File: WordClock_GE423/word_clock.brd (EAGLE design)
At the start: 100 x 76.2 mm, 45 parts, among them Q1 32.768kHz

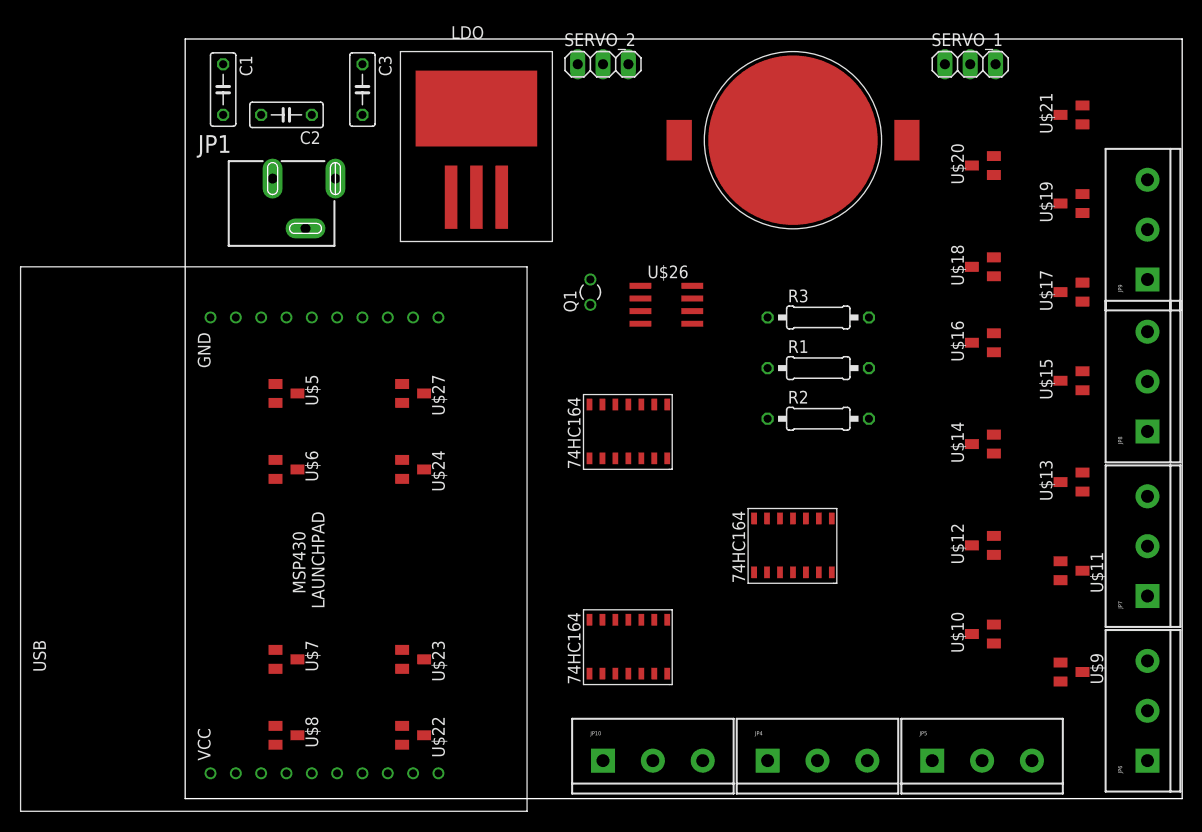
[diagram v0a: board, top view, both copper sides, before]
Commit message: finished boards
finally. added VCC rail for LEDs
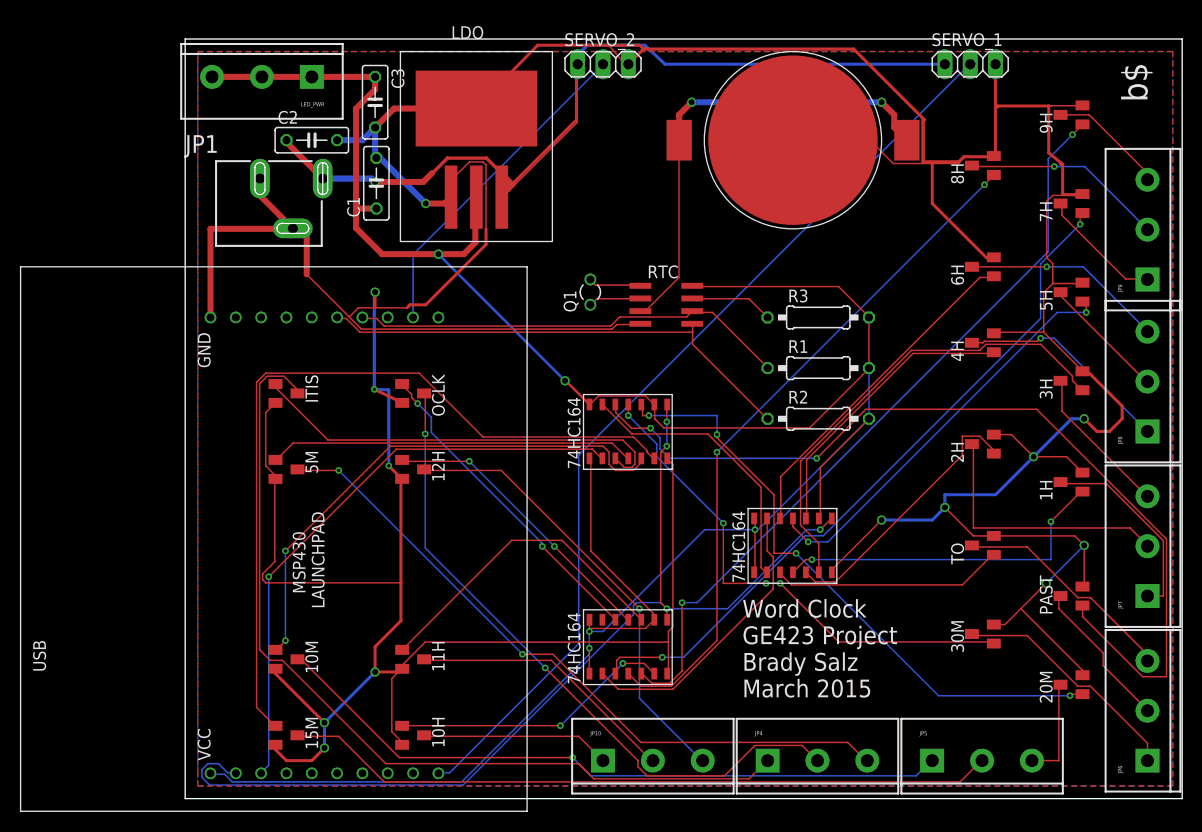
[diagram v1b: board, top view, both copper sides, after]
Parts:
- removed U$11, U$9: FET, word_clock:SOT23
- added 20M, PAST: FET, word_clock:SOT23
- added LED_PWR: (no value), SparkFun-Connectors:SCREWTERMINAL-5MM-3
- moved C1 18.0 mm to (19.2, 61.7), turned to 90 degrees
- moved C2 3.59 mm to (12.7, 66.0), turned to 0 degrees
- moved C3 1.80 mm to (19.1, 69.8)
- moved JP1 1.27 mm to (0.00, 64.8)
- renumbered U$10 to 30M, U$12 to TO, U$13 to 1H, U$14 to 2H, U$15 to 3H, U$16 to 4H, U$17 to 5H, U$18 to 6H, U$19 to 7H, U$20 to 8H, U$21 to 9H, U$22 to 10H, U$23 to 11H, U$24 to 12H, U$26 to RTC, U$27 to OCLK, U$5 to ITIS, U$6 to 5M, U$7 to 10M, U$8 to 15M
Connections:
- net 3.3V: now also LED_PWR.1, LED_PWR.2, LED_PWR.3
- net GND: now also 20M.2, PAST.2; no longer U$11.2, U$9.2
- net PAST: now also PAST.1; no longer U$11.1
- net PAST_LED: now also PAST.3; no longer U$11.3
- net TWENTY: now also 20M.1; no longer U$9.1
- net TWENTY_LED: now also 20M.3; no longer U$9.3
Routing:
- net GND: track 0.00 -> 617.9 mm, vias 0 -> 13
- net 3.3V: track 0.00 -> 266.1 mm, vias 0 -> 5
- net VCC_5: track 0.00 -> 110.8 mm, vias 0 -> 1
- net SR_CLK: track 0.00 -> 102.5 mm, vias 0 -> 4
- net SERVO_1: track 0.00 -> 93.9 mm
- net PAST: track 0.00 -> 91.9 mm, vias 0 -> 2
- net IT_IS_LED: track 0.00 -> 88.8 mm
- net QUARTER: track 0.00 -> 79.2 mm
- net NINE: track 0.00 -> 77.3 mm, vias 0 -> 2
- net QUARTER_LED: track 0.00 -> 71.5 mm
- net SEVEN: track 0.00 -> 70.4 mm, vias 0 -> 2
- net EIGHT: track 0.00 -> 69.5 mm, vias 0 -> 2
- net FIVE_MIN_LED: track 0.00 -> 69.3 mm, vias 0 -> 2
- net TEN_MIN_LED: track 0.00 -> 69.2 mm, vias 0 -> 1
- net OCLK_LED: track 0.00 -> 66.6 mm, vias 0 -> 2
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- added copper zone on layer 1, net GND
- added copper zone on layer 16, net GND
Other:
- board text added: "Word Clock GE423 Project Brady Salz March 2015"
- board text added: "b$"
